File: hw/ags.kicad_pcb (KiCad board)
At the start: 2 copper layers, 77 x 66.5 mm, 123 parts, among them J1 Screw_Terminal_01x08, J2 SWD/ARM10, J3 Conn_02x03_Odd_Even, J9 Screw_Terminal_01x02, SW1 PTS526SM15SMTR2 LFS, U1 GAQY212GSX, U10 GAQY212GSX, U11 GAQY212GSX, U12 NV24C08DWVLT3G, U2 GAQY212GSX, U3 GAQY212GSX, U4 LMR51610XDBVR, U5 ESP32-S3-MINI-1, U6 GAQY212GSX, U7 GAQY212GSX, U9 GAQY212GSX

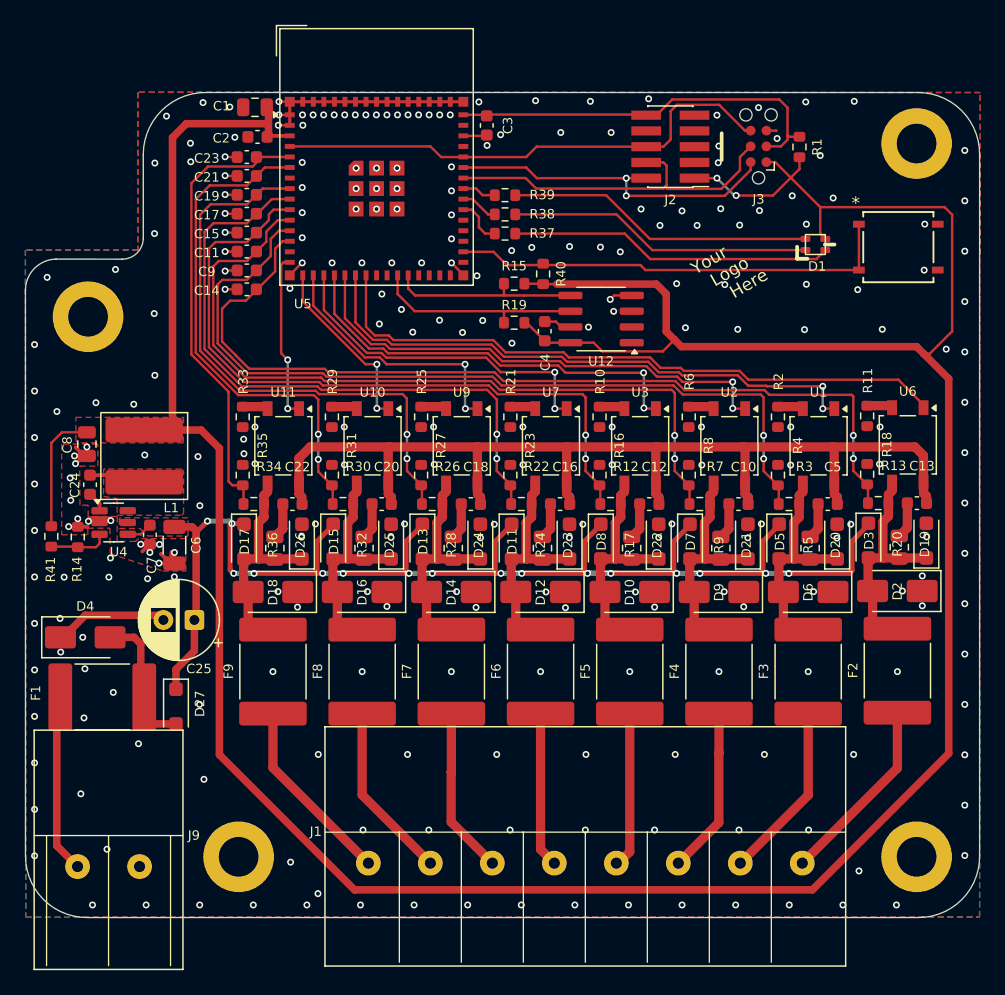
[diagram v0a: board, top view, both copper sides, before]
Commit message: Added spare pins breakout to header, cleaned up silk
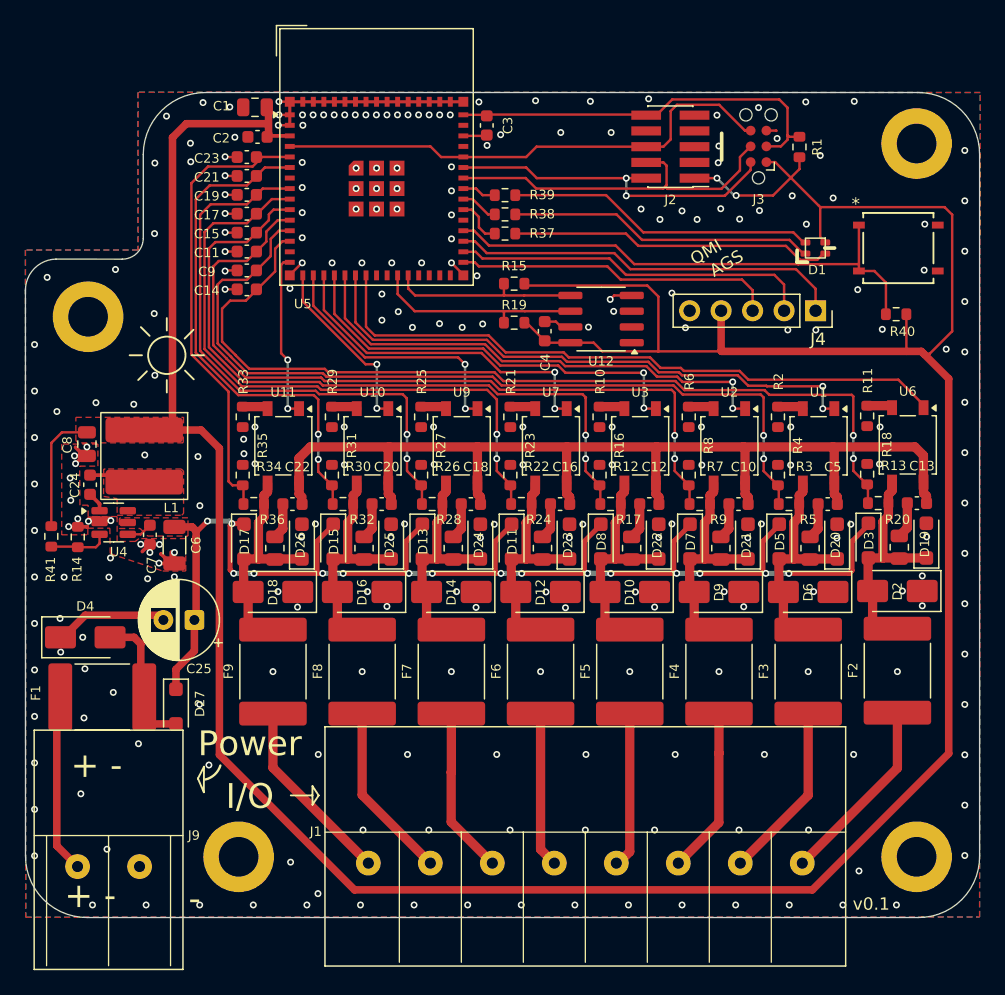
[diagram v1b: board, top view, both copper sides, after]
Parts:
- added J4: Conn_01x05, Connector_PinSocket_2.54mm:PinSocket_1x05_P2.54mm_Vertical, F.Cu at (158.7, 102.1)
- moved R40 28.7 mm to (165.2, 102.3), turned to 0 degrees
- moved D1 0.28 mm to (158.7, 97.0)
- moved SW1 0.07 mm to (165.4, 97.0)
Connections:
- R40 pad 1: Net-(U5-IO36) -> Net-(U5-IO38)
- SW1 pad 1: Net-(U5-IO36) -> Net-(U5-IO38)
- SW1 pad 2: Net-(U5-IO36) -> Net-(U5-IO38)
- U5 pad 31: unconnected-(U5-IO35-Pad31) -> /Spare_1
- U5 pad 32: Net-(U5-IO36) -> /Spare_2
- U5 pad 33: unconnected-(U5-IO37-Pad33) -> /Spare_3
- U5 pad 34: unconnected-(U5-IO38-Pad34) -> Net-(U5-IO38)
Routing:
- net Net-(U5-IO38): track 0.00 -> 41.9 mm
- net Net-(U5-IO36): track 36.2 -> 0.00 mm
- net /Spare_3: track 0.00 -> 31.8 mm
- net /Spare_2: track 0.00 -> 29.1 mm
- net /Spare_1: track 0.00 -> 25.9 mm
- net +3.3V: track 275.6 -> 283.0 mm
- net GND: vias 270 -> 262
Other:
- board text added: "+ -"
- board text added: "-"
- board text added: "I/O"
- board text added: "Power"
- board text added: "QMI AGS"
- board text added: "QMI Innovation Inc. Automatic Generator Start 5-60V DC 1W"
- board text added: "v0.1"
- board text removed: "Your Logo Here"

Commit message: Added sense for input voltage and created BOM
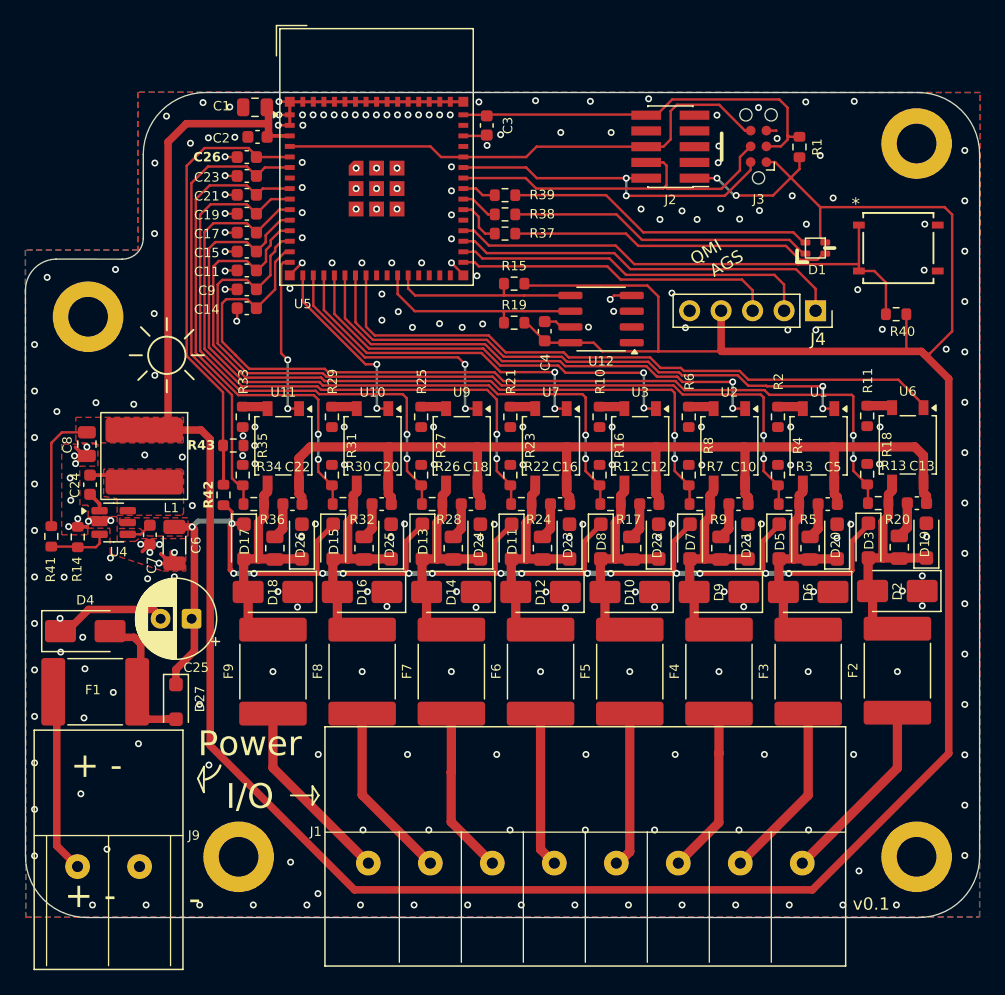
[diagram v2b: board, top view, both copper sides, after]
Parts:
- added C26: 2.7n, Capacitor_SMD:C_0603_1608Metric, F.Cu at (112.9, 89.7)
- added R42: 113k 1%, Resistor_SMD:R_0603_1608Metric, F.Cu at (111.0, 116.9)
- added R43: 5.90k 1%, Resistor_SMD:R_0603_1608Metric, F.Cu at (111.8, 112.9)
- C10, C12, C13, C16, C18, C20, C22, C5: value 1u -> 1u 60V
- C25: value 22u -> 22u 80V
- moved C11 1.52 mm to (112.9, 98.8)
- moved C14 1.52 mm to (112.9, 101.9)
- moved C15 1.52 mm to (112.9, 97.3)
- moved C17 1.52 mm to (112.9, 95.8)
- moved C19 1.52 mm to (112.9, 94.2)
- moved C23 1.52 mm to (112.9, 91.2)
- moved C9 1.52 mm to (112.9, 100.3)
- moved C21 1.52 mm to (112.9, 92.7)
- moved F1 0.72 mm to (100.6, 132.8)
- moved D4 0.50 mm to (99.8, 127.9)
- moved D27 0.38 mm to (107.1, 133.6)
- moved C25 0.25 mm to (108.4, 126.9)
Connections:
- U5 pad 10: /SENSE_4 -> /SENSE_5
- U5 pad 11: /SENSE_3 -> /SENSE_4
- U5 pad 12: /SENSE_2 -> /SENSE_3
- U5 pad 13: /SENSE_1 -> /SENSE_2
- U5 pad 14: unconnected-(U5-IO10-Pad14) -> /SENSE_1
- U5 pad 5: /SENSE_8 -> /SENSE_VIN
- U5 pad 6: /SENSE_7 -> /SENSE_8
- U5 pad 8: /SENSE_6 -> /SENSE_7
- U5 pad 9: /SENSE_5 -> /SENSE_6
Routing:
- net /SENSE_VIN: track 0.00 -> 36.2 mm
- net Net-(D27-A): track 9.45 -> 11.8 mm
- net +V: track 108.0 -> 109.4 mm
- net GND: track 63.2 -> 64.7 mm, vias 262 -> 264
- net /SENSE_3: track 62.4 -> 63.3 mm
- net /SENSE_1: track 73.3 -> 74.0 mm
- net /SENSE_4: track 56.9 -> 57.5 mm
- net /SENSE_2: track 68.1 -> 68.6 mm
- net /SENSE_6: track 46.1 -> 46.6 mm

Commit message: Fixed button footprint and layout, fixed IO0 layout, widened connector holes
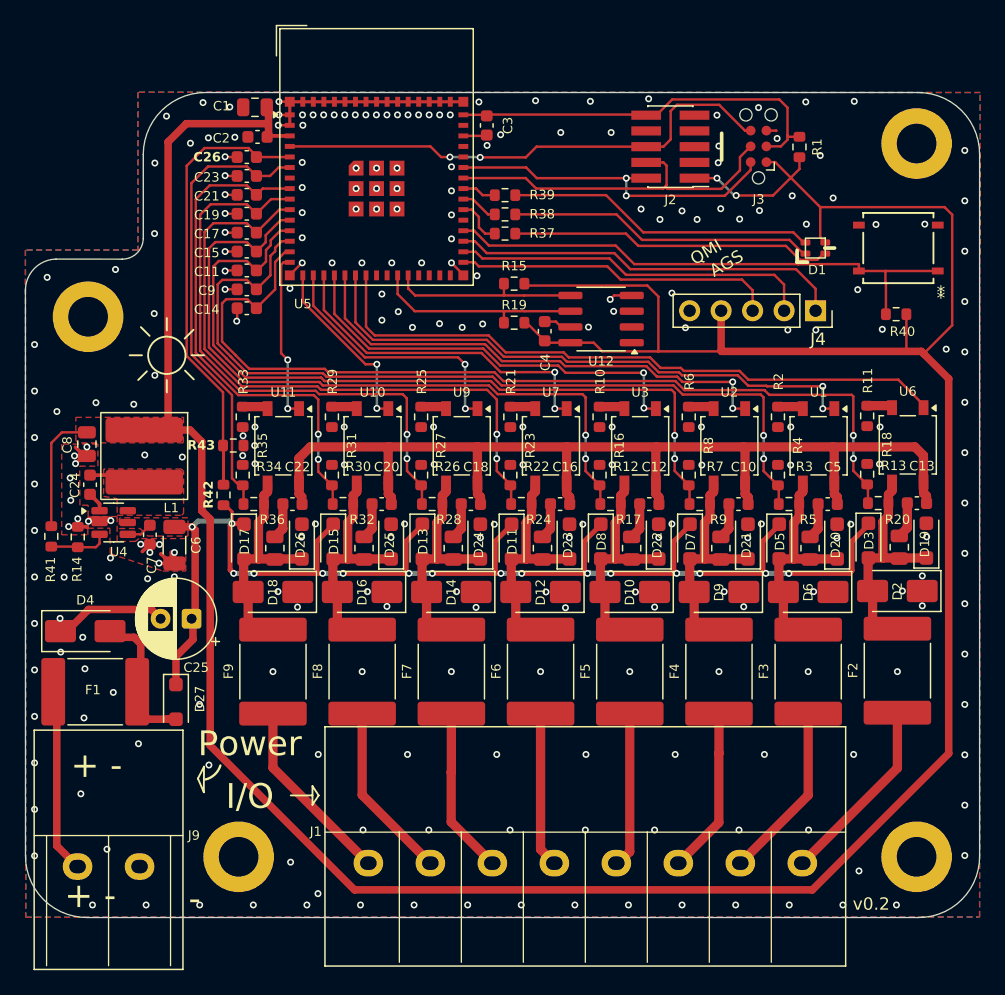
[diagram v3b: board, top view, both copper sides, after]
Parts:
- turned SW1 to 180 degrees
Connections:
- U5 pad 41: /IO0 -> unconnected-(U5-IO45-Pad41)
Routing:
- net +3.3V: track 282.8 -> 279.9 mm
- net Net-(U5-IO38): track 41.9 -> 43.4 mm
- net GND: track 64.7 -> 64.4 mm, vias 264 -> 263
- net /IO0: vias 0 -> 2
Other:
- board text added: "v0.2"
- board text removed: "v0.1"
